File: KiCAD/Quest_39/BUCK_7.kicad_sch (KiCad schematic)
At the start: 21 parts

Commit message: Fixed most ERC errors
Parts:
- gave numbers to parts that had none: 21
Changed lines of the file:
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@@
   (symbol (lib_id "Analog_ADC:INA226") (at 78.74 73.66 0) (unit 1)
     (in_bom yes) (on_board yes)
-    (property "Reference" "U?" (id 0) (at 83.82 62.23 0)
+    (property "Reference" "U33" (id 0) (at 83.82 62.23 0)
       (effects (font (size 1.27 1.27)) (justify left))
     )
@@
   (symbol (lib_id "Device:C_Polarized") (at 86.36 46.99 0) (unit 1)
     (in_bom yes) (on_board yes) (fields_autoplaced)
-    (property "Reference" "C?" (id 0) (at 90.17 44.8309 0)
+    (property "Reference" "C101" (id 0) (at 90.17 44.8309 0)
       (effects (font (size 1.27 1.27)) (justify left))
     )
@@
   (symbol (lib_id "Device:C_Polarized") (at 393.7 172.72 0) (unit 1)
     (in_bom yes) (on_board yes)
-    (property "Reference" "C?" (id 0) (at 397.4895 171.4075 0)
+    (property "Reference" "C111" (id 0) (at 397.4895 171.4075 0)
       (effects (font (size 1.27 1.27)) (justify left))
     )
@@
   (symbol (lib_id "Device:C") (at 55.88 55.88 90) (unit 1)
     (in_bom yes) (on_board yes)
-    (property "Reference" "C?" (id 0) (at 55.88 52.07 90))
+    (property "Reference" "C105" (id 0) (at 55.88 52.07 90))
     (property "Value" "1uF" (id 1) (at 55.88 59.69 90))
     (property "Footprint" "OptoDevice:R_LDR_4.9x4.2mm_P2.54mm_Vertical" (id 2) (at 59.69 54.9148 0)
@@
   (symbol (lib_id "MCP4151:MCP4151-502E{slash}SN") (at 254 220.98 0) (unit 1)
     (in_bom yes) (on_board yes)
-    (property "Reference" "U?" (id 0) (at 312.42 214.63 0)
+    (property "Reference" "U35" (id 0) (at 312.42 214.63 0)
       (effects (font (size 1.524 1.524)))
     )
@@
   (symbol (lib_id "Device:C_Polarized") (at 381 172.72 0) (unit 1)
     (in_bom yes) (on_board yes)
-    (property "Reference" "C?" (id 0) (at 384.7895 171.4075 0)
+    (property "Reference" "C110" (id 0) (at 384.7895 171.4075 0)
       (effects (font (size 1.27 1.27)) (justify left))
     )
@@
   (symbol (lib_id "Device:C_Polarized") (at 354.33 172.72 0) (unit 1)
     (in_bom yes) (on_board yes)
-    (property "Reference" "C?" (id 0) (at 358.1195 171.4075 0)
+    (property "Reference" "C108" (id 0) (at 358.1195 171.4075 0)
       (effects (font (size 1.27 1.27)) (justify left))
     )
@@
   (symbol (lib_id "Device:C") (at 100.33 46.99 0) (unit 1)
     (in_bom yes) (on_board yes) (fields_autoplaced)
-    (property "Reference" "C?" (id 0) (at 104.14 45.7199 0)
+    (property "Reference" "C102" (id 0) (at 104.14 45.7199 0)
       (effects (font (size 1.27 1.27)) (justify left))
     )
@@
   (symbol (lib_id "Device:C") (at 113.03 46.99 0) (unit 1)
     (in_bom yes) (on_board yes) (fields_autoplaced)
-    (property "Reference" "C?" (id 0) (at 116.84 45.7199 0)
+    (property "Reference" "C103" (id 0) (at 116.84 45.7199 0)
       (effects (font (size 1.27 1.27)) (justify left))
     )
@@
   (symbol (lib_id "Amplifier_Operational:MCP601-xOT") (at 35.56 66.04 0) (unit 1)
     (in_bom yes) (on_board yes)
-    (property "Reference" "U?" (id 0) (at 38.1 62.23 0))
+    (property "Reference" "U32" (id 0) (at 38.1 62.23 0))
     (property "Value" "MCP601T-I/OT" (id 1) (at 41.91 69.85 0))
     (property "Footprint" "Package_TO_SOT_SMD:SOT-23-5" (id 2) (at 33.02 71.12 0)
@@
   (symbol (lib_id "Device:C") (at 335.28 172.72 0) (unit 1)
     (in_bom yes) (on_board yes) (fields_autoplaced)
-    (property "Reference" "C?" (id 0) (at 339.09 171.4499 0)
+    (property "Reference" "C107" (id 0) (at 339.09 171.4499 0)
       (effects (font (size 1.27 1.27)) (justify left))
     )
@@
   (symbol (lib_id "Device:R") (at 60.96 49.53 0) (unit 1)
     (in_bom yes) (on_board yes) (fields_autoplaced)
-    (property "Reference" "R?" (id 0) (at 63.5 48.2599 0)
+    (property "Reference" "R45" (id 0) (at 63.5 48.2599 0)
       (effects (font (size 1.27 1.27)) (justify left))
     )
@@
   (symbol (lib_id "Device:C") (at 128.27 137.16 0) (unit 1)
     (in_bom yes) (on_board yes) (fields_autoplaced)
-    (property "Reference" "C?" (id 0) (at 132.08 135.8899 0)
+    (property "Reference" "C106" (id 0) (at 132.08 135.8899 0)
       (effects (font (size 1.27 1.27)) (justify left))
     )
@@
   (symbol (lib_id "Device:C") (at 337.82 224.79 0) (unit 1)
     (in_bom yes) (on_board yes) (fields_autoplaced)
-    (property "Reference" "C?" (id 0) (at 341.63 223.5199 0)
+    (property "Reference" "C112" (id 0) (at 341.63 223.5199 0)
       (effects (font (size 1.27 1.27)) (justify left))
     )
@@
   (symbol (lib_id "Device:R") (at 55.88 41.91 90) (unit 1)
     (in_bom yes) (on_board yes) (fields_autoplaced)
-    (property "Reference" "R?" (id 0) (at 55.88 35.56 90))
+    (property "Reference" "R43" (id 0) (at 55.88 35.56 90))
     (property "Value" "0R0025" (id 1) (at 55.88 38.1 90))
     (property "Footprint" "" (id 2) (at 55.88 43.688 90)
@@
   (symbol (lib_id "Device:C_Polarized") (at 368.3 172.72 0) (unit 1)
     (in_bom yes) (on_board yes)
-    (property "Reference" "C?" (id 0) (at 372.0895 171.4075 0)
+    (property "Reference" "C109" (id 0) (at 372.0895 171.4075 0)
       (effects (font (size 1.27 1.27)) (justify left))
     )
@@
   (symbol (lib_id "LTM4611EV:LTM4611EV-PBF") (at 132.08 102.87 0) (unit 1)
     (in_bom yes) (on_board yes)
-    (property "Reference" "U?" (id 0) (at 308.61 50.8 0)
+    (property "Reference" "U34" (id 0) (at 308.61 50.8 0)
       (effects (font (size 1.524 1.524)))
     )
@@
   (symbol (lib_id "Device:R") (at 322.58 215.9 0) (unit 1)
     (in_bom yes) (on_board yes) (fields_autoplaced)
-    (property "Reference" "R?" (id 0) (at 325.12 214.6299 0)
+    (property "Reference" "R47" (id 0) (at 325.12 214.6299 0)
       (effects (font (size 1.27 1.27)) (justify left))
     )
@@
   (symbol (lib_id "Device:C") (at 125.73 46.99 0) (unit 1)
     (in_bom yes) (on_board yes) (fields_autoplaced)
-    (property "Reference" "C?" (id 0) (at 129.54 45.7199 0)
+    (property "Reference" "C104" (id 0) (at 129.54 45.7199 0)
       (effects (font (size 1.27 1.27)) (justify left))
     )
@@
   (symbol (lib_id "Device:R") (at 127 91.44 0) (unit 1)
     (in_bom yes) (on_board yes) (fields_autoplaced)
-    (property "Reference" "R?" (id 0) (at 129.54 90.1699 0)
+    (property "Reference" "R46" (id 0) (at 129.54 90.1699 0)
       (effects (font (size 1.27 1.27)) (justify left))
     )
@@
   (symbol (lib_id "Device:R") (at 48.26 49.53 0) (unit 1)
     (in_bom yes) (on_board yes) (fields_autoplaced)
-    (property "Reference" "R?" (id 0) (at 50.8 48.2599 0)
-      (effects (font (size 1.27 1.27)) (justify left))
-    )
+    (property "Reference" "R44" (id 0) (at 50.8 48.2599 0)
+      (effects (font (size 1.27 1.27)) (justify left))
+    )

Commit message: Gave all INA226's unique addresses
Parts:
- removed C101: 330uF, symbol Device:C_Polarized
- removed C102, C103, C104: 22uF, symbol Device:C
- removed C105: 1uF, OptoDevice:R_LDR_4.9x4.2mm_P2.54mm_Vertical, symbol Device:C
- removed C106, C112: 100nF, symbol Device:C
- removed C107: 100pF, symbol Device:C
- removed C108, C109, C110, C111: 100uF, symbol Device:C_Polarized
- removed R43: 0R0025, symbol Device:R
- removed R44, R45: 10, symbol Device:R
- removed R46: 10K, symbol Device:R
- removed R47: 20K, symbol Device:R
- removed U32: MCP601T-I/OT, Package_TO_SOT_SMD:SOT-23-5, symbol Amplifier_Operational:MCP601-xOT
- added C112: 330uF, symbol Device:C_Polarized
- added C113, C114, C115: 22uF, symbol Device:C
- added C116: 1uF, OptoDevice:R_LDR_4.9x4.2mm_P2.54mm_Vertical, symbol Device:C
- added C117, C118, C125: 100nF, symbol Device:C
- added C119: 10nF, symbol Device:C
- added C120, C121, C122, C123: 100uF, symbol Device:C_Polarized
- added C124: 100pF, symbol Device:C
- added R66: 0R0025, symbol Device:R
- added R67, R68: 10R, symbol Device:R
- added R69: 9k, symbol Device:R
- added R70: 1k, symbol Device:R
- added R71: 10k, symbol Device:R
- added R72: 20K, symbol Device:R
- added TP55, TP56, TP57, TP58, TP59, TP60, TP61: TestPoint, symbol Connector:TestPoint
- added U32: AD626ANZ, N_8_ADI, symbol AD626ANZ:AD626ANZ
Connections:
- net +5V: now also U33.1 (A1), C118.1, C125.1, U32.6 (+VS)
- net GND: now also C117.2, C118.2, C125.2, U32.2 (AGND), U32.3 (-VS); no longer U33.1 (A1), U33.2 (A0), U33.3 (~{Alert})
- net NEG: now also C112.2, C113.2, C114.2, C115.2, C119.1, C120.2, C121.2, C122.2, C123.2, R70.2, U32.1 (-IN); no longer U33.8 (Vbus)
- net P0A: now also R72.2
- net POS: now also C120.1, C121.1, C122.1, C123.1, C124.1
- net PV_POS: now also U34.A1 (VIN), U34.A2 (VIN), U34.A3 (VIN), U34.A4 (VIN), U34.A5 (VIN), U34.A6 (VIN), U34.B1 (VIN), U34.B2 (VIN), U34.B3 (VIN), U34.B4 (VIN), U34.B5 (VIN), U34.B6 (VIN), U34.C1 (VIN), U34.C2 (VIN), U34.C3 (VIN), U34.C4 (VIN), U34.C5 (VIN), U34.C6 (VIN), C112.1, C113.1, C114.1, C115.1, R66.1, R66.2, R67.1, R68.1, R69.1, R71.1
- net RUN: now also R71.2
- net SCL: now also U33.2 (A0)
- net TRACK/SS: now also C119.2
- net Vfb: now also C124.2, R72.1
- net Vin+: now also C116.1, R67.2
- net Vin-: now also U33.8 (Vbus), U33.9 (Vin-), C116.2, R68.2, TP56.1, U32.5 (OUT)
- net at U34.A11 (COMP): now also TP59.1
- net at U34.A7 (INTVCC): now also U34.D9 (INTVCC), TP55.1
- net at U34.B12 (PLLFLTR/FSET): now also TP58.1
- net at U34.F11 (PGOOD): now also U34.G12 (PGOOD), TP57.1
- net at U34.K12 (DIFFVOUT), U34.L12 (VOUT_LCL): now also TP60.1, TP61.1
- new net: C117.1, U32.4 (FILTER)
- new net +IN: R69.2, R70.1, U32.8 (+IN)
- no-connect marks 16 -> 12
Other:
- note added: "10:1 divider"
- note added: "Addr=0x47"
- note added: "Extra mounting"
- note added: "G=10"
- note added: "Output voltage is set by varying Rfb with a digipot. SPI = 00"
- note added: "the measured voltage is divided and then amplified by 10 as to simulate a follower. This is done to make use of the AD626 (low price and availability)."

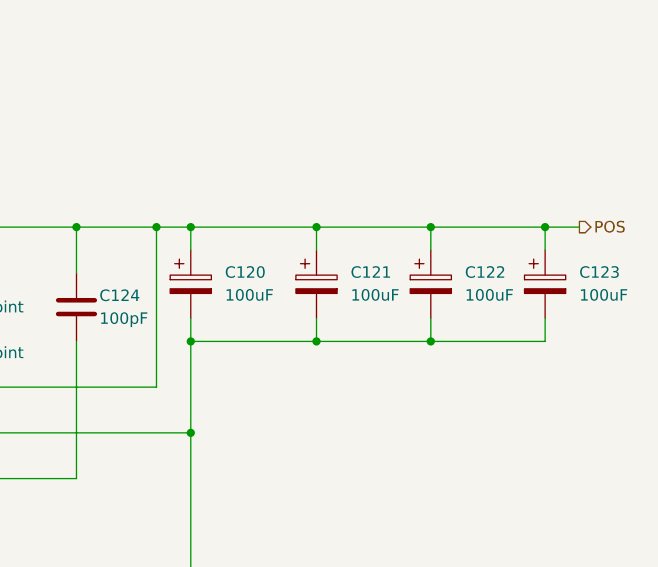
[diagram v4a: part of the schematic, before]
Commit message: Assigned all schem. symbols their footprints
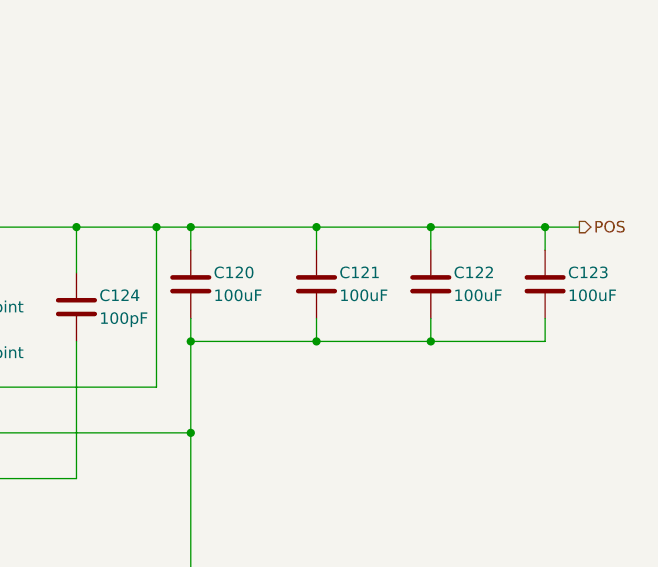
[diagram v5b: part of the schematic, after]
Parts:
- removed C120, C121, C122, C123: 100uF, symbol Device:C_Polarized
- added C120, C121, C122, C123: 100uF, Capacitor_SMD:C_1206_3216Metric, symbol Device:C
- C112: footprint (none) -> Capacitor_SMD:CP_Elec_8x6.9
- C113, C114, C115, C117, C118, C119, C124, C125: footprint (none) -> Capacitor_SMD:C_0805_2012Metric
- C116: footprint OptoDevice:R_LDR_4.9x4.2mm_P2.54mm_Vertical -> Capacitor_SMD:C_0805_2012Metric
- R66: footprint (none) -> Resistor_SMD:R_1206_3216Metric
- R67, R68, R69, R70, R71, R72: footprint (none) -> Resistor_SMD:R_0805_2012Metric
- TP55, TP56, TP57, TP58, TP59, TP60, TP61: footprint (none) -> TestPoint:TestPoint_Pad_D2.0mm
- U32: footprint N_8_ADI -> Package_DIP:DIP-8_W7.62mm_Socket_LongPads
- U34: footprint LGA-133_3_LIT -> Package_LGA:Linear_LGA-133_15.0x15.0mm_Layout12x12_P1.27mm
- U35: footprint SOIC8-N_MC_MCH -> Package_SO:MSOP-8_3x3mm_P0.65mm
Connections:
- net NEG: now also C120.2, C121.2, C122.2, C123.2
- net POS: now also C120.1, C121.1, C122.1, C123.1

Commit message: Initial work on layout
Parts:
- C116, C117, C118, C119, C124, C125: footprint Capacitor_SMD:C_0805_2012Metric -> Capacitor_SMD:C_0603_1608Metric
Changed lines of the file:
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@@
     (property "Reference" "C116" (id 0) (at 74.93 59.69 90))
     (property "Value" "1uF" (id 1) (at 74.93 67.31 90))
-    (property "Footprint" "Capacitor_SMD:C_0805_2012Metric" (id 2) (at 78.74 62.5348 0)
+    (property "Footprint" "Capacitor_SMD:C_0603_1608Metric" (id 2) (at 78.74 62.5348 0)
       (effects (font (size 1.27 1.27)) hide)
     )
@@
       (effects (font (size 1.27 1.27)) (justify left))
     )
-    (property "Footprint" "Capacitor_SMD:C_0805_2012Metric" (id 2) (at 345.1352 171.45 0)
+    (property "Footprint" "Capacitor_SMD:C_0603_1608Metric" (id 2) (at 345.1352 171.45 0)
       (effects (font (size 1.27 1.27)) hide)
     )
@@
       (effects (font (size 1.27 1.27)) (justify left))
     )
-    (property "Footprint" "Capacitor_SMD:C_0805_2012Metric" (id 2) (at 341.3252 223.52 0)
+    (property "Footprint" "Capacitor_SMD:C_0603_1608Metric" (id 2) (at 341.3252 223.52 0)
       (effects (font (size 1.27 1.27)) hide)
     )
@@
       (effects (font (size 1.27 1.27)) (justify left))
     )
-    (property "Footprint" "Capacitor_SMD:C_0805_2012Metric" (id 2) (at 106.3752 127 0)
+    (property "Footprint" "Capacitor_SMD:C_0603_1608Metric" (id 2) (at 106.3752 127 0)
       (effects (font (size 1.27 1.27)) hide)
     )
@@
       (effects (font (size 1.27 1.27)) (justify left))
     )
-    (property "Footprint" "Capacitor_SMD:C_0805_2012Metric" (id 2) (at 64.4652 85.09 0)
+    (property "Footprint" "Capacitor_SMD:C_0603_1608Metric" (id 2) (at 64.4652 85.09 0)
       (effects (font (size 1.27 1.27)) hide)
     )
@@
       (effects (font (size 1.27 1.27)) (justify left))
     )
-    (property "Footprint" "Capacitor_SMD:C_0805_2012Metric" (id 2) (at 26.3652 83.82 0)
-      (effects (font (size 1.27 1.27)) hide)
-    )
+    (property "Footprint" "Capacitor_SMD:C_0603_1608Metric" (id 2) (at 26.3652 83.82 0)
+      (effects (font (size 1.27 1.27)) hide)
+    )

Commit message: Fixed INA226 schem. mistake and further layout work
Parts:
- added C123: 100nF, Capacitor_SMD:C_0603_1608Metric, symbol Device:C
- renumbered C112 to C119, C113 to C120, C114 to C121, C115 to C122, C116 to C124, C117 to C125, C118 to C126, C119 to C127, C120 to C128, C121 to C129, C122 to C130, C123 to C131, C124 to C132, C125 to C133
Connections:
- net +5V: now also C123.1
- net GND: now also C123.2
- net PV_POS: no longer C119.1, C120.1, C121.1, C122.1, R66.2, R68.1, R71.1, U34.A1 (VIN), U34.A2 (VIN), U34.A3 (VIN), U34.A4 (VIN), U34.A5 (VIN), U34.A6 (VIN), U34.B1 (VIN), U34.B2 (VIN), U34.B3 (VIN), U34.B4 (VIN), U34.B5 (VIN), U34.B6 (VIN), U34.C1 (VIN), U34.C2 (VIN), U34.C3 (VIN), U34.C4 (VIN), U34.C5 (VIN), U34.C6 (VIN)
- net Vin-: no longer TP56.1, U32.5 (OUT), U33.8 (Vbus)
- new net: TP56.1, U32.5 (OUT), U33.8 (Vbus)
- new net BUCK_VIN: C119.1, C120.1, C121.1, C122.1, R66.2, R68.1, R71.1, U34.A1 (VIN), U34.A2 (VIN), U34.A3 (VIN), U34.A4 (VIN), U34.A5 (VIN), U34.A6 (VIN), U34.B1 (VIN), U34.B2 (VIN), U34.B3 (VIN), U34.B4 (VIN), U34.B5 (VIN), U34.B6 (VIN), U34.C1 (VIN), U34.C2 (VIN), U34.C3 (VIN), U34.C4 (VIN), U34.C5 (VIN), U34.C6 (VIN)

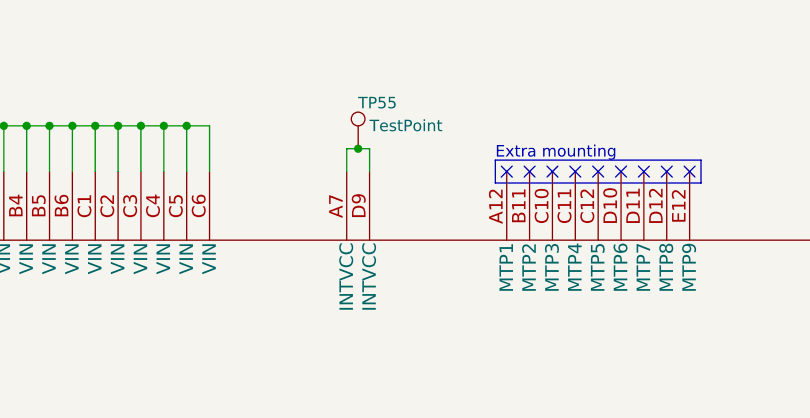
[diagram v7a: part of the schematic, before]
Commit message: Partial wiring of first buck converter section PCB layout
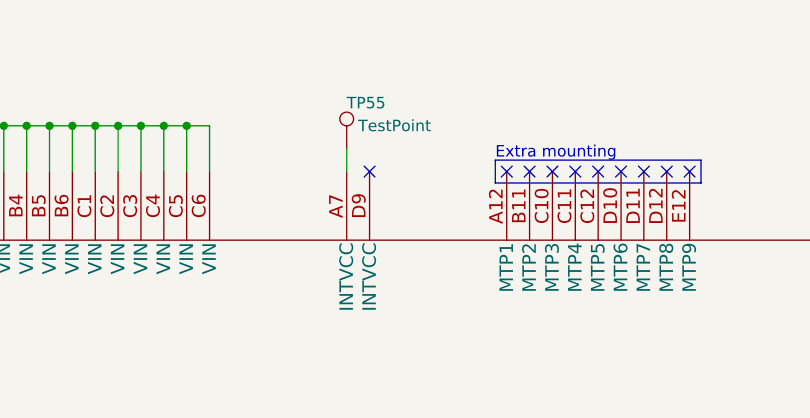
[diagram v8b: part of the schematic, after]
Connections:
- net at TP55.1, U34.A7 (INTVCC): no longer U34.D9 (INTVCC)
- no-connect marks 12 -> 13
